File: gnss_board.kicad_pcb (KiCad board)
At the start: 2 copper layers, 58 parts, among them J1 Conn_01x10_Pin, U1 H1102NL, U2 LAN8710A, U3 TPS2375D, U4 TX4138(ESOIC-8)

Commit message: Update connector
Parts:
- added C15: 22uF, Capacitor_SMD:C_0805_2012Metric, F.Cu at (114.1, 91.4)
- added FET1: WPM2015-3/TR, Package_TO_SOT_SMD:SOT-23_Handsoldering, F.Cu at (108.7, 86.5)
- added R26: 10k, Resistor_SMD:R_0805_2012Metric, F.Cu at (114.1, 85.5)
- added R27: 1K, Resistor_SMD:R_0805_2012Metric, F.Cu at (114.1, 88.5)
- added T1: LMUN2211LT1G, Package_TO_SOT_SMD:SOT-23_Handsoldering, F.Cu at (108.7, 91.3)
- J1: footprint Connector_JST:JST_SH_BM10B-SRSS-TB_1x10-1MP_P1.00mm_Vertical -> Connector_Molex:Molex_PicoBlade_53398-1071_1x10-1MP_P1.25mm_Vertical
- TVS1: value ESDS314DBVR(SOT-23-5) -> ESDS314DBVR
- TVS2, TVS3: value D_TVS -> GG0603052R542P

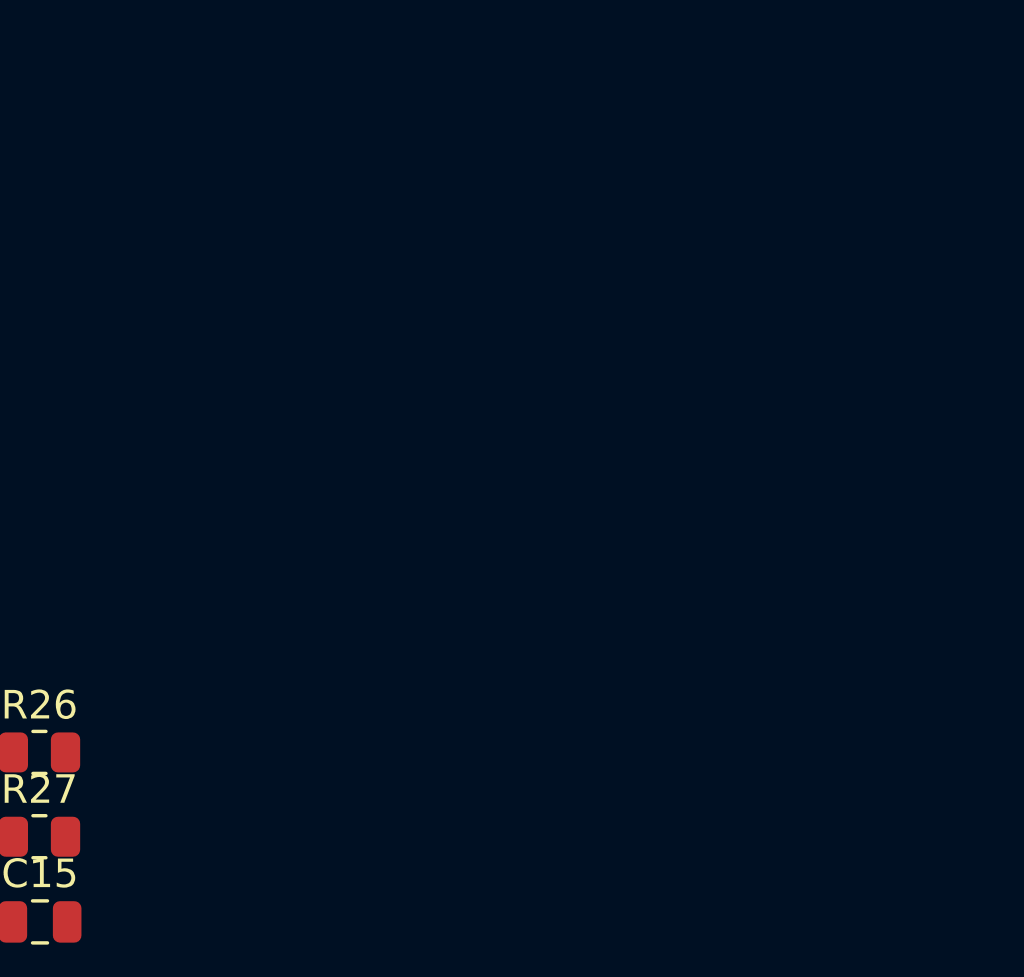
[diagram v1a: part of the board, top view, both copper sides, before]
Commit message: Add power supply to ESP32
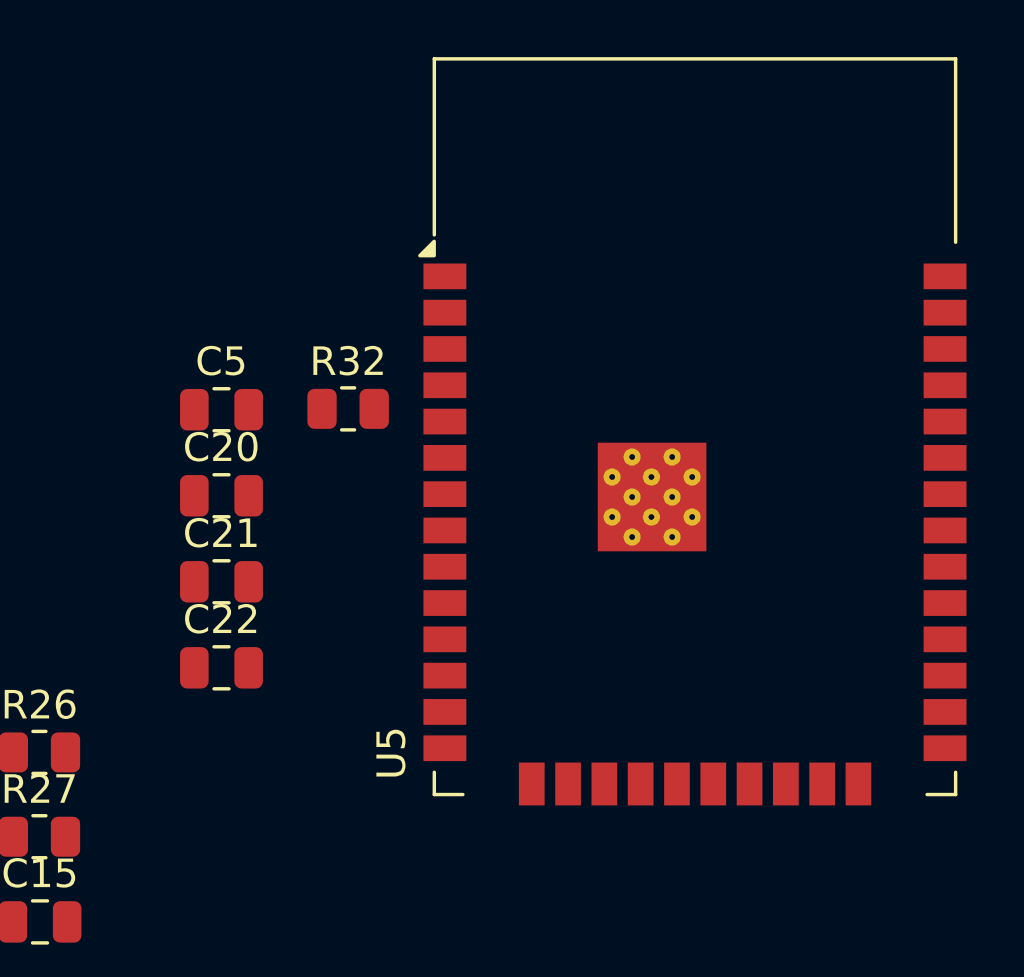
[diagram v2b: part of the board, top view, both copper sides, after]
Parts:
- added C20: 0.1uF, Capacitor_SMD:C_0805_2012Metric, F.Cu at (120.5, 76.5)
- added C21: 22uF, Capacitor_SMD:C_0805_2012Metric, F.Cu at (120.5, 79.5)
- added C22: 1uF, Capacitor_SMD:C_0805_2012Metric, F.Cu at (120.5, 82.5)
- added C5: 100nF, Capacitor_SMD:C_0805_2012Metric, F.Cu at (120.5, 73.5)
- added R32: 10K, Resistor_SMD:R_0805_2012Metric, F.Cu at (124.9, 73.5)
- added U5: ESP32-WROOM-32E, RF_Module:ESP32-WROOM-32D, F.Cu at (137.0, 77.1)

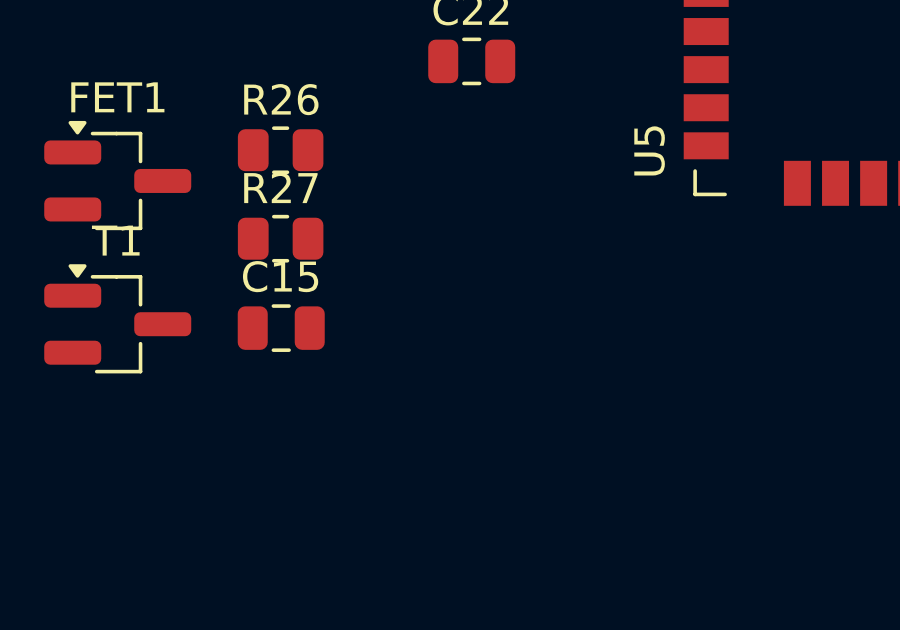
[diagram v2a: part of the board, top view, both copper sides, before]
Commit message: Connect ESP32 to the LAN chip
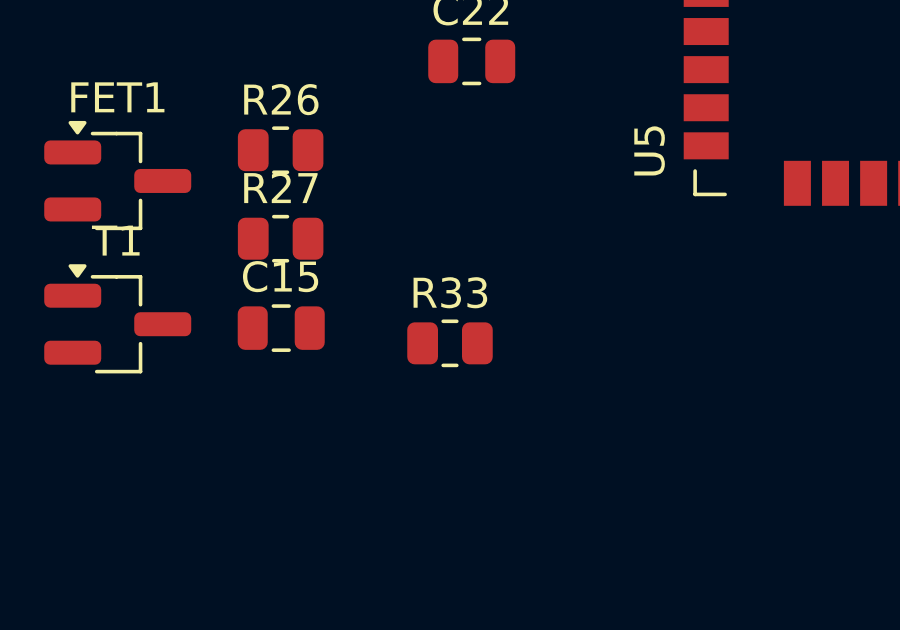
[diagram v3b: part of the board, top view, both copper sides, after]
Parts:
- added R33: 10K, Resistor_SMD:R_0805_2012Metric, F.Cu at (119.7, 91.9)
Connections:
- net Net-(U5-EN) renamed ESP_EN
- R12 pad 1: RXD0 -> ETH_RXD0
- R13 pad 1: RXD1 -> ETH_RXD1
- R18 pad 1: RX_CRS_DV -> ETH_RX_CRS_DV
- R19 pad 1: MDIO -> ETH_MDIO
- T1 pad 1: PHY_PWR -> ETH_PHY_PWR
- U2 pad 10: RXD1 -> ETH_RXD1
- U2 pad 11: RXD0 -> ETH_RXD0
- U2 pad 15: RX_CRS_DV -> ETH_RX_CRS_DV
- U2 pad 16: MDIO -> ETH_MDIO
- U2 pad 17: MDC -> ETH_MDC
- U2 pad 21: TX_EN -> ETH_TX_EN
- U2 pad 22: TXD0 -> ETH_TXD0
- U2 pad 23: TXD1 -> ETH_TXD1
- U2 pad 5: CLK_OUT -> ETH_CLK_IN
- U5 pad 10: unconnected-(U5-IO25-Pad10) -> ETH_RXD0
- U5 pad 11: unconnected-(U5-IO26-Pad11) -> ETH_RXD1
- U5 pad 12: unconnected-(U5-IO27-Pad12) -> ETH_RX_CRS_DV
- U5 pad 14: unconnected-(U5-IO12-Pad14) -> ETH_PHY_PWR
- U5 pad 25: unconnected-(U5-IO0-Pad25) -> ESP_IO0
- U5 pad 28: unconnected-(U5-IO17-Pad28) -> ETH_CLK_IN
- U5 pad 30: unconnected-(U5-IO18-Pad30) -> ETH_MDIO
- U5 pad 31: unconnected-(U5-IO19-Pad31) -> ETH_TXD0
- U5 pad 33: unconnected-(U5-IO21-Pad33) -> ETH_TX_EN
- U5 pad 34: unconnected-(U5-RXD0/IO3-Pad34) -> ESP_RXD0
- U5 pad 35: unconnected-(U5-TXD0/IO1-Pad35) -> ESP_TXD0
- U5 pad 36: unconnected-(U5-IO22-Pad36) -> ETH_TXD1
- U5 pad 37: unconnected-(U5-IO23-Pad37) -> ETH_MDC

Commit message: Add Serial Connector for programming
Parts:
- added J2: Serial Connector, Connector_PinHeader_2.54mm:PinHeader_1x06_P2.54mm_Vertical, F.Cu at (134.4, 97.3)
- added Q1: BC817, Package_TO_SOT_SMD:SOT-23, F.Cu at (139.1, 97.4)
- added Q2: BC817, Package_TO_SOT_SMD:SOT-23, F.Cu at (139.1, 102.0)
- added R34: 1K, Resistor_SMD:R_0805_2012Metric, F.Cu at (138.9, 105.7)
- added R35: 1K, Resistor_SMD:R_0805_2012Metric, F.Cu at (138.9, 108.6)

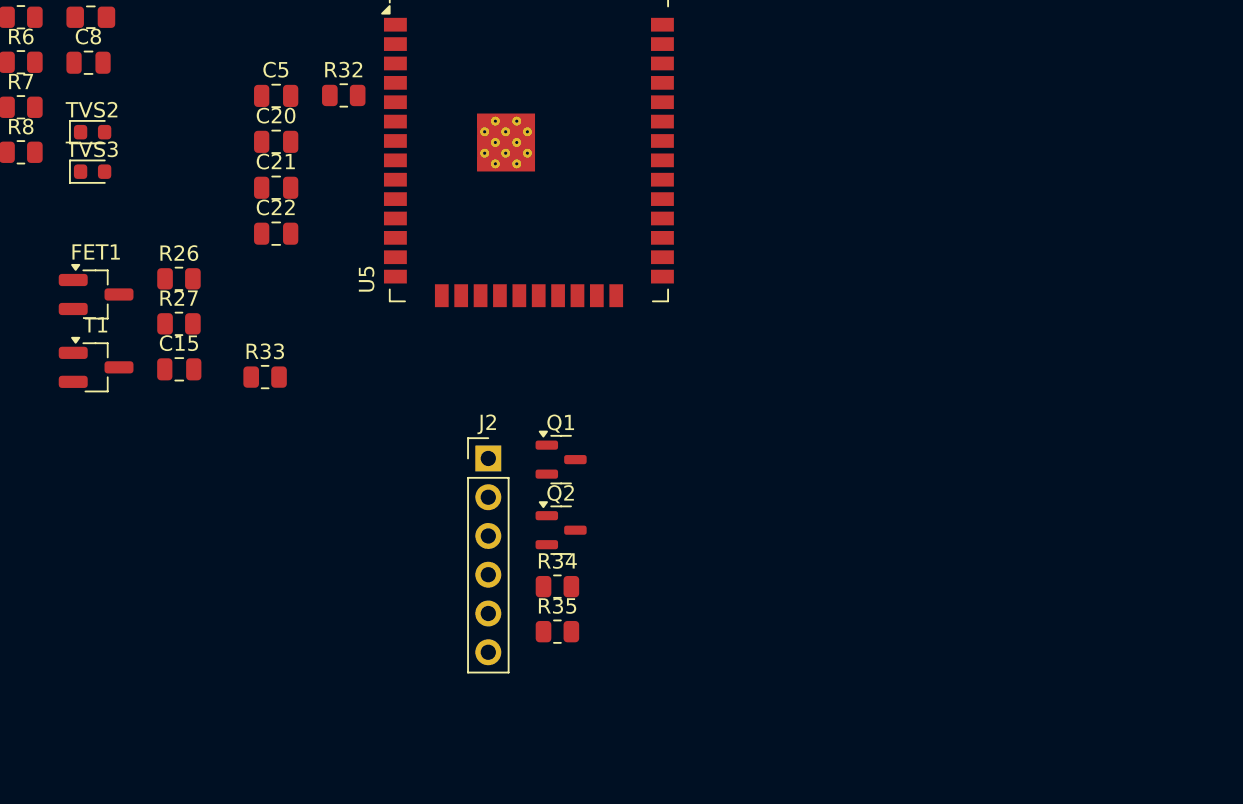
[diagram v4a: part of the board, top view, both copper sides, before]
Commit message: Add GNSS module as well
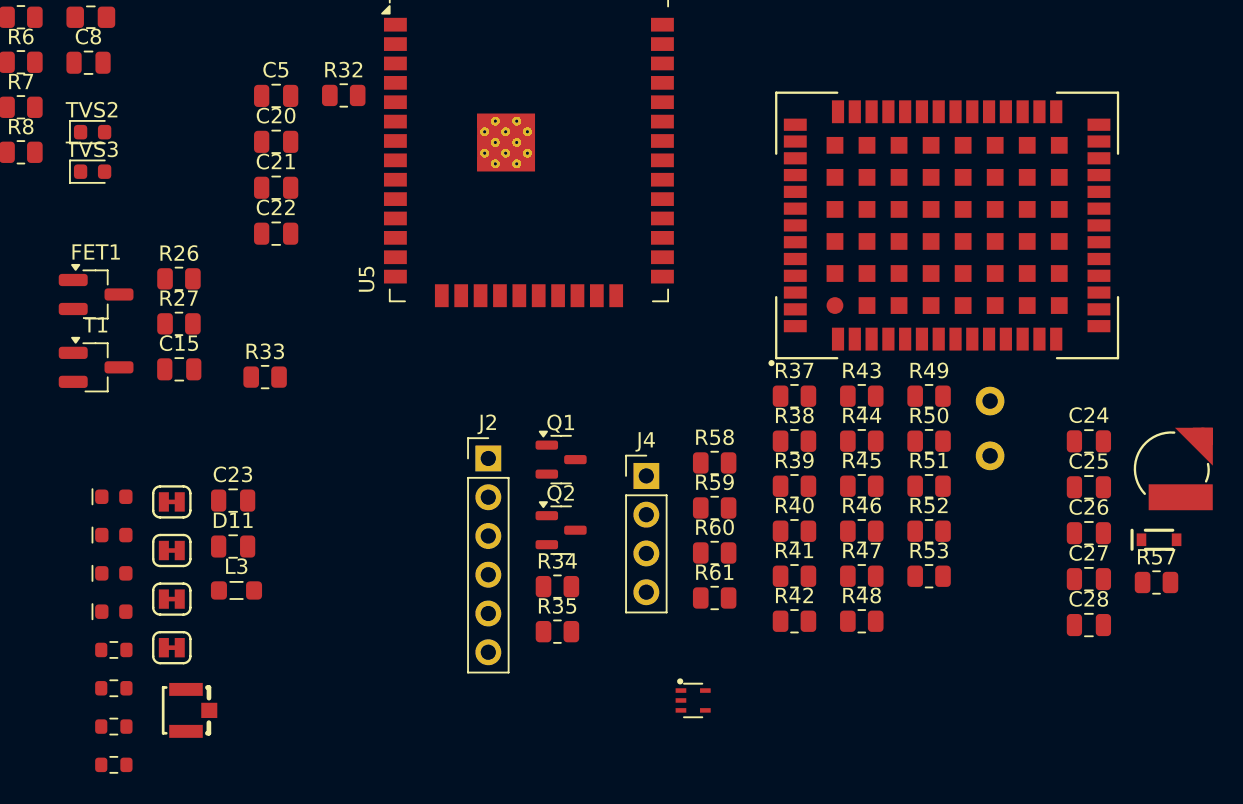
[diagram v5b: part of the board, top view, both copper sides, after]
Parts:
- added BT1: 6.8mm, SparkFun-Battery:ML414H_IV01E, F.Cu at (179.1, 98.0)
- added C23: 100pF, Capacitor_SMD:C_0805_2012Metric, F.Cu at (117.6, 100.0)
- added C24: 0.1uF, Capacitor_SMD:C_0805_2012Metric, F.Cu at (173.7, 96.2)
- added C25: 100pF, Capacitor_SMD:C_0805_2012Metric, F.Cu at (173.7, 99.2)
- added C26: 2.2uF, Capacitor_SMD:C_0805_2012Metric, F.Cu at (173.7, 102.2)
- added C27: 100nF, Capacitor_SMD:C_0805_2012Metric, F.Cu at (173.7, 105.2)
- added C28: 1uF, Capacitor_SMD:C_0805_2012Metric, F.Cu at (173.7, 108.2)
- added D10: PMEG4005EJ, SparkFun-Semiconductor-Standard:SOD-323, F.Cu at (178.3, 102.6)
- added D11: PESD0805, Capacitor_SMD:C_0805_2012Metric, F.Cu at (117.6, 103.1)
- added D12: PESD3V3L4UG, SparkFun-Semiconductor-Standard:SOT-353, F.Cu at (147.8, 113.1)
- added D4: Red, SparkFun-LED:LED_0603_1608Metric_Red, F.Cu at (109.8, 99.8)
- added D7: Yellow, SparkFun-LED:LED_0603_1608Metric_Yellow, F.Cu at (109.8, 102.3)
- added D8: Blue, SparkFun-LED:LED_0603_1608Metric_Blue, F.Cu at (109.8, 104.8)
- added D9: White, SparkFun-LED:LED_0603_1608Metric_White, F.Cu at (109.8, 107.3)
- added J3: U.FL, SparkFun-Connector:U.FL, F.Cu at (114.6, 113.8)
- added J4: Conn_01x04_Pin, Connector_PinHeader_2.54mm:PinHeader_1x04_P2.54mm_Vertical, F.Cu at (144.7, 98.4)
- added JP2: ~, SparkFun-Jumper:Jumper_2_NC_Trace, F.Cu at (113.6, 100.1)
- added JP3: ~, SparkFun-Jumper:Jumper_2_NC_Trace, F.Cu at (113.6, 103.3)
- added JP4: ~, SparkFun-Jumper:Jumper_2_NC_Trace, F.Cu at (113.6, 106.5)
- added JP5: ~, SparkFun-Jumper:Jumper_2_NC_Trace, F.Cu at (113.6, 109.7)
- added L3: 68nH, Inductor_SMD:L_0805_2012Metric_Pad1.05x1.20mm_HandSolder, F.Cu at (117.9, 105.9)
- added R36: 1k, SparkFun-Resistor:R_0603_1608Metric, F.Cu at (109.8, 109.8)
- added R37: 10K, Resistor_SMD:R_0805_2012Metric, F.Cu at (154.4, 93.2)
- added R38: 33R, Resistor_SMD:R_0805_2012Metric, F.Cu at (154.4, 96.2)
- added R39: 10K, Resistor_SMD:R_0805_2012Metric, F.Cu at (154.4, 99.1)
- added R40: 33R, Resistor_SMD:R_0805_2012Metric, F.Cu at (154.4, 102.0)
- added R41: 33R, Resistor_SMD:R_0805_2012Metric, F.Cu at (154.4, 105.0)
- added R42: 33R, Resistor_SMD:R_0805_2012Metric, F.Cu at (154.4, 108.0)
- added R43: 33R, Resistor_SMD:R_0805_2012Metric, F.Cu at (158.8, 93.2)
- added R44: 33R, Resistor_SMD:R_0805_2012Metric, F.Cu at (158.8, 96.2)
- added R45: 33R, Resistor_SMD:R_0805_2012Metric, F.Cu at (158.8, 99.1)
- added R46: 33R, Resistor_SMD:R_0805_2012Metric, F.Cu at (158.8, 102.0)
- added R47: 33R, Resistor_SMD:R_0805_2012Metric, F.Cu at (158.8, 105.0)
- added R48: 33R, Resistor_SMD:R_0805_2012Metric, F.Cu at (158.8, 108.0)
- added R49: 33R, Resistor_SMD:R_0805_2012Metric, F.Cu at (163.3, 93.2)
- added R50: 33R, Resistor_SMD:R_0805_2012Metric, F.Cu at (163.3, 96.2)
- added R51: 33R, Resistor_SMD:R_0805_2012Metric, F.Cu at (163.3, 99.1)
- added R52: 33R, Resistor_SMD:R_0805_2012Metric, F.Cu at (163.3, 102.0)
- added R53: 10K, Resistor_SMD:R_0805_2012Metric, F.Cu at (163.3, 105.0)
- added R54: 2.2k, SparkFun-Resistor:R_0603_1608Metric, F.Cu at (109.8, 112.3)
- added R55: 2.2k, SparkFun-Resistor:R_0603_1608Metric, F.Cu at (109.8, 114.9)
- added R56: 1k, SparkFun-Resistor:R_0603_1608Metric, F.Cu at (109.8, 117.4)
- added R57: 1K, Resistor_SMD:R_0805_2012Metric, F.Cu at (178.2, 105.4)
- added R58: 1K, Resistor_SMD:R_0805_2012Metric, F.Cu at (149.2, 97.6)
- added R59: 2.2K, Resistor_SMD:R_0805_2012Metric, F.Cu at (149.2, 100.5)
- added R60: 2.2K, Resistor_SMD:R_0805_2012Metric, F.Cu at (149.2, 103.5)
- added R61: 1K, Resistor_SMD:R_0805_2012Metric, F.Cu at (149.2, 106.4)
- added TP1: PTH, SparkFun-Connector:1x01, F.Cu at (167.3, 93.5)
- added TP2: PTH, SparkFun-Connector:1x01, F.Cu at (167.3, 97.1)
- added U6: UM980, SparkFun-GPS:UM980, F.Cu at (164.4, 82.0)
- U1: footprint GNSS Board:H11X_PUL -> gnss_board:H11X_PUL
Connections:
- U5 pad 13: unconnected-(U5-IO14-Pad13) -> GNSS_TXD1
- U5 pad 23: unconnected-(U5-IO15-Pad23) -> GNSS_RXD1
- U5 pad 6: unconnected-(U5-IO34-Pad6) -> GNSS_TXD2
- U5 pad 7: unconnected-(U5-IO35-Pad7) -> GNSS_RXD2
